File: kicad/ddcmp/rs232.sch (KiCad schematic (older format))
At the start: 14 parts, among them J5 DTE, J6 DCE, U3 MAX3222, U4 MAX3222

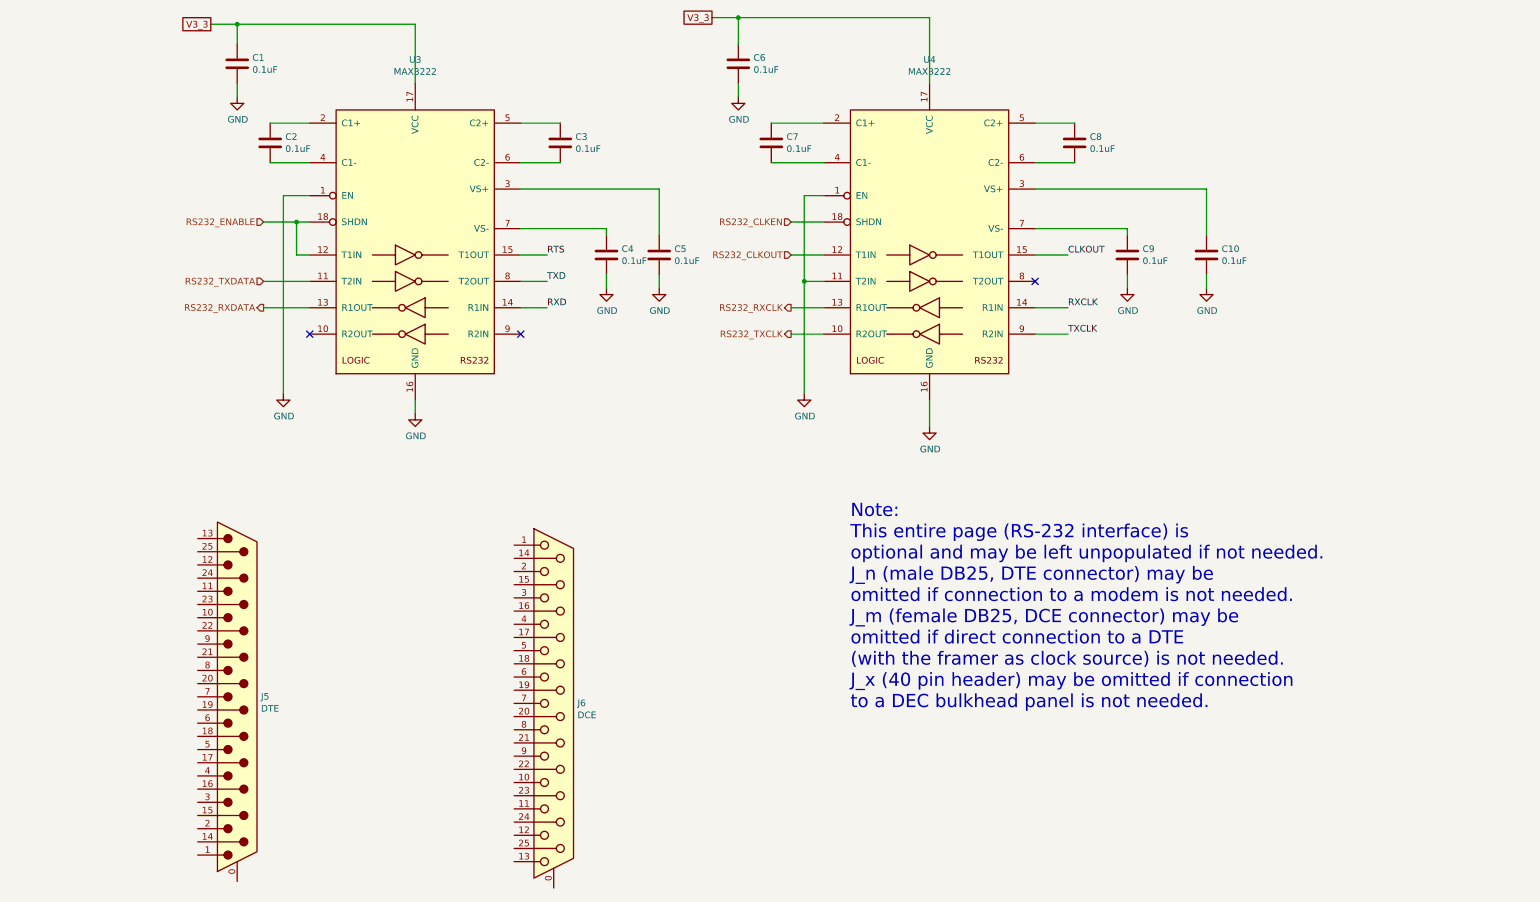
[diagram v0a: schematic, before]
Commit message: Finish the connector hookups, to be verified carefully against DMR-11 schematics.
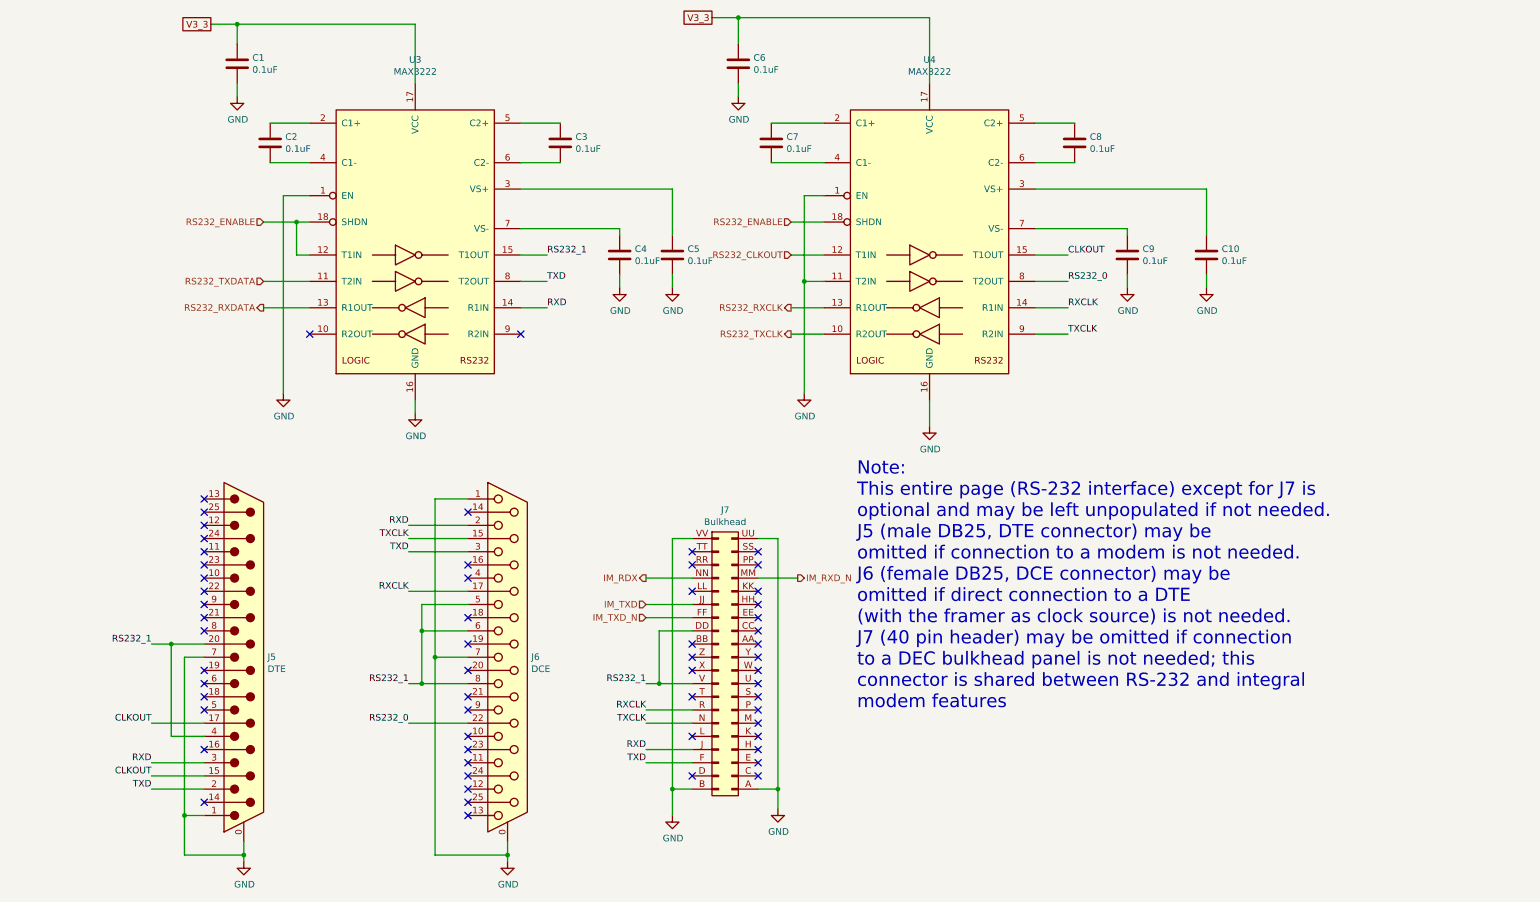
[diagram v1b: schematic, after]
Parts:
- added J7: Bulkhead, ddcmp_parts:Berg_40_pin_DEC_pinout, symbol ddcmp_symbols:Berg_40_pin_DEC_labeling
- J5: footprint (none) -> ddcmp_parts:Amphenol_DB25M_PCB
- J6: footprint (none) -> ddcmp_parts:Amphenol_DB25F_PCB
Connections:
- net RS232_CLKEN is gone; now on net RS232_ENABLE: U4.18 (SHDN)
- net RTS is gone; now on net RS232_1: U3.15 (T1OUT)
- net CLKOUT: now also J5.15 (P15), J5.17 (P17)
- net GND: now also J5.0 (PAD), J5.1, J5.7, J6.0 (PAD), J6.1, J6.7, J7.A (Pin_40), J7.B (Pin_39), J7.UU (Pin_2), J7.VV (Pin_1)
- net RXCLK: now also J6.17 (P17), J7.R (Pin_27)
- net RXD: now also J5.3, J6.2, J7.J (Pin_33)
- net TXCLK: now also J6.15 (P15), J7.N (Pin_29)
- net TXD: now also J5.2, J6.3, J7.F (Pin_35)
- net RS232_0: now reaches U4.8 (T2OUT)
- net RS232_0: now also J6.22 (P22)
- net RS232_1: now reaches J5.20 (P20)
- net RS232_1: now also J5.4, J6.5, J6.6, J6.8, J7.DD (Pin_15), J7.V (Pin_23)
- new net IM_RDX: J7.NN (Pin_7)
- new net IM_RXD_N: J7.MM (Pin_8)
- new net IM_TXD: J7.JJ (Pin_11)
- new net IM_TXD_N: J7.FF (Pin_13)
- no-connect marks 3 -> 60
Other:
- note added: "Note:\nThis entire page (RS-232 interface) except for J7 is \noptional and may be left unpopulated if not needed.\nJ5 (male DB25, DTE connector) may be \nomitted if connection to a modem is not needed.\nJ6 (female DB25, DCE connector) may be \nomitted if direct connection to a DTE\n(with the framer as clock source) is not needed.\nJ7 (40 pin header) may be omitted if connection \nto a DEC bulkhea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"
- note removed: "Note:\nThis entire page (RS-232 interface) is \noptional and may be left unpopulated if not needed.\nJ_n (male DB25, DTE connector) may be \nomitted if connection to a modem is not needed.\nJ_m (female DB25, DCE connector) may be \nomitted if direct connection to a DTE\n(with the framer as clock source) is not needed.\nJ_x (40 pin header) may be omitted if connection \nto a DEC bulkhead panel is 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"
- moved on the sheet: C4, C5, J5, J6

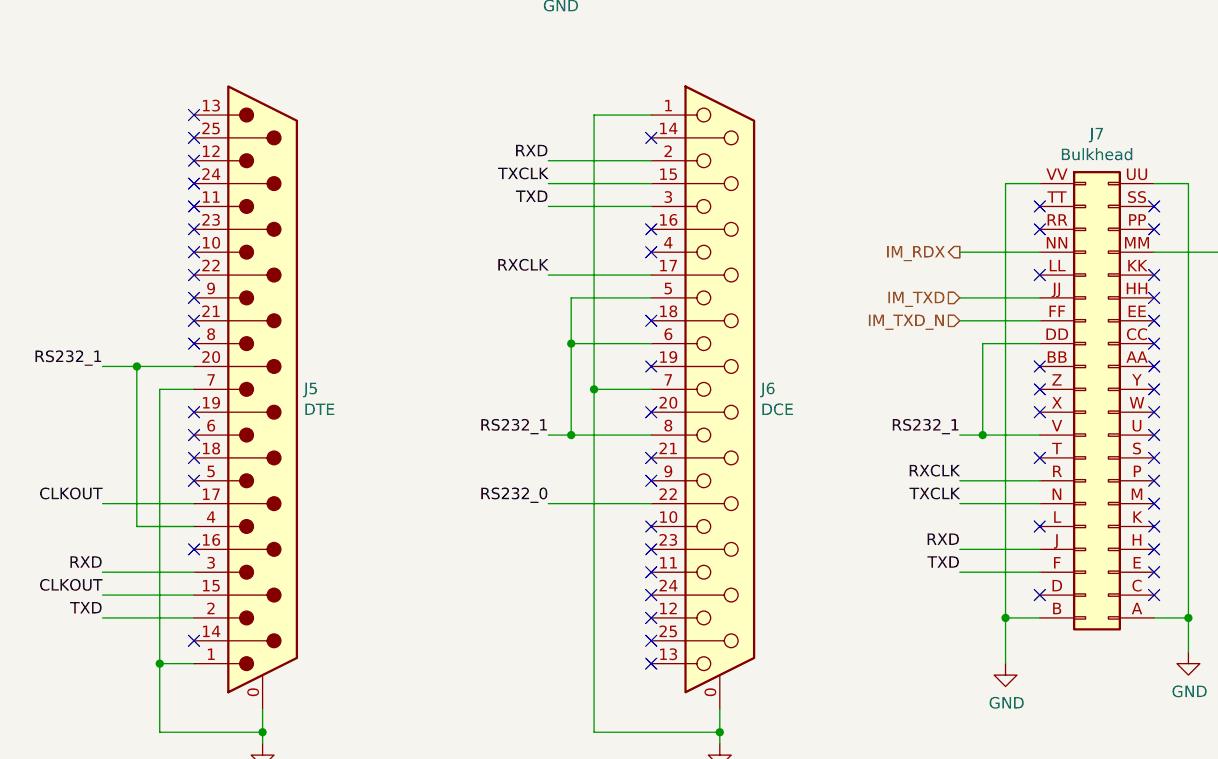
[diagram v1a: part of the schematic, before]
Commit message: Complete schematic, PCB layout, and matching code.  Needs testing.
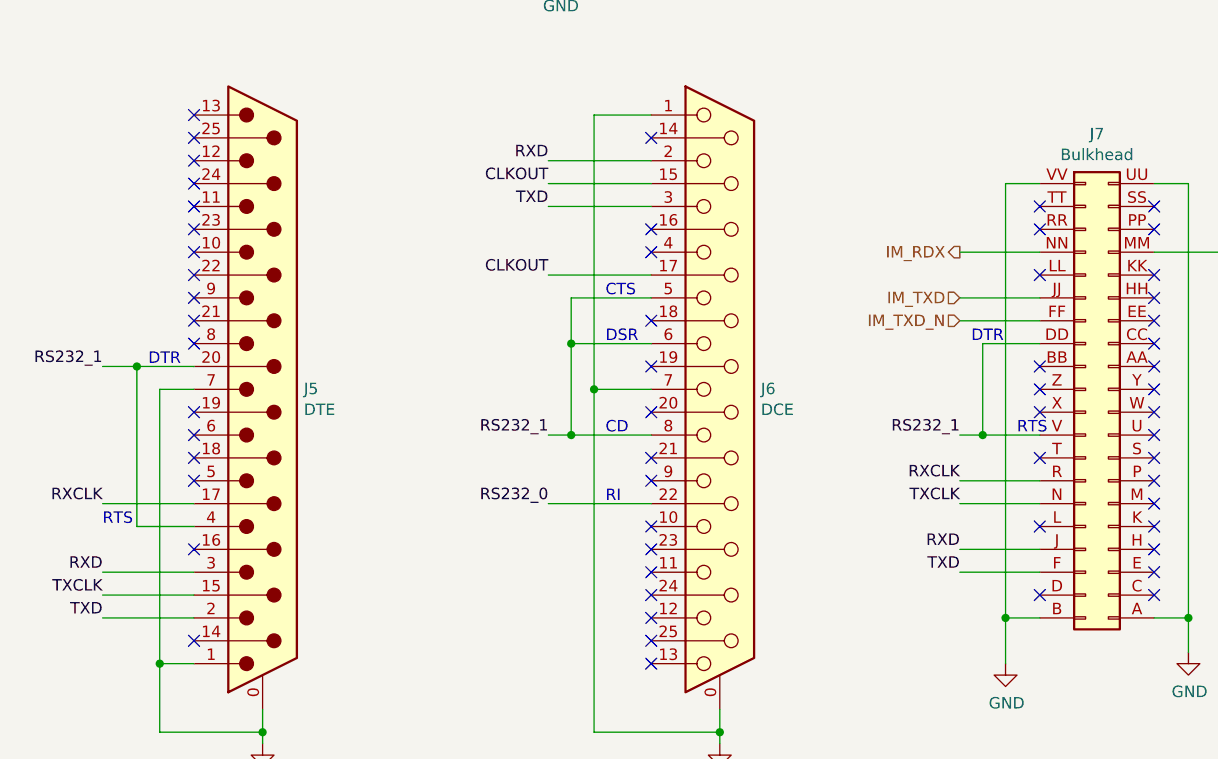
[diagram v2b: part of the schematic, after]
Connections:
- net CLKOUT: now also J6.15 (P15), J6.17 (P17); no longer J5.15 (P15), J5.17 (P17)
- net RXCLK: now also J5.17 (P17); no longer J6.17 (P17)
- net TXCLK: now also J5.15 (P15); no longer J6.15 (P15)
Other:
- note added: "CD"
- note added: "CTS"
- note added: "DSR"
- note added: "DTR"
- note added: "RI"
- note added: "RTS"
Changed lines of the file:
@@
 Rev "A"
 Comp "AK Design"
-Comment1 ""
+Comment1 "Copyright © 2021 by Paul Koning, NI1D"
 Comment2 ""
 Comment3 ""
@@
 Wire Wire Line
 	2100 6550 1700 6550
-Text Label 1700 6550 2    50   ~ 0
-CLKOUT
 Wire Wire Line
 	2100 6150 1700 6150
-Text Label 1700 6150 2    50   ~ 0
-CLKOUT
 Wire Wire Line
 	4100 5150 3650 5150
 Wire Wire Line
 	4100 4750 3650 4750
-Text Label 3650 4750 2    50   ~ 0
-TXCLK
-Text Label 3650 5150 2    50   ~ 0
-RXCLK
 NoConn ~ 4100 4550
 NoConn ~ 4100 4950
@@
 Wire Wire Line
 	5650 6650 5650 6850
+Text Label 1700 6550 2    50   ~ 0
+TXCLK
+Text Label 1700 6150 2    50   ~ 0
+RXCLK
+Text Label 3650 4750 2    50   ~ 0
+CLKOUT
+Text Label 3650 5150 2    50   ~ 0
+CLKOUT
+Text Notes 1700 6250 0    50   ~ 0
+RTS
+Text Notes 1900 5550 0    50   ~ 0
+DTR
+Text Notes 5500 5450 0    50   ~ 0
+DTR
+Text Notes 5700 5850 0    50   ~ 0
+RTS
+Text Notes 3900 5850 0    50   ~ 0
+CD
+Text Notes 3900 5450 0    50   ~ 0
+DSR
+Text Notes 3900 5250 0    50   ~ 0
+CTS
+Text Notes 3900 6150 0    50   ~ 0
+RI
 $EndSCHEMATC
